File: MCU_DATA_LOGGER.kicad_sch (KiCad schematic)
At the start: 25 parts, among them U1 DS1337S+, U2 24LC1025, U3 24LC1025, U4 ATMEGA328P-AU, Y1 32.768 KHz, Y2 16 MHz

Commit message: fixed all issues
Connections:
- net Vcc: now also BT1.1 (+), C5.1, D3.2 (A), U4.18 (AVCC), U4.4 (VCC)
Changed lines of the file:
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@@
     (effects (font (size 1.27 1.27) bold) (justify right bottom))
+  )
+  (label "Vcc" (at 241.3 43.18 0)
+    (effects (font (size 1.27 1.27) bold) (justify left bottom))
   )
   (label "MOSI" (at 223.52 144.78 180)

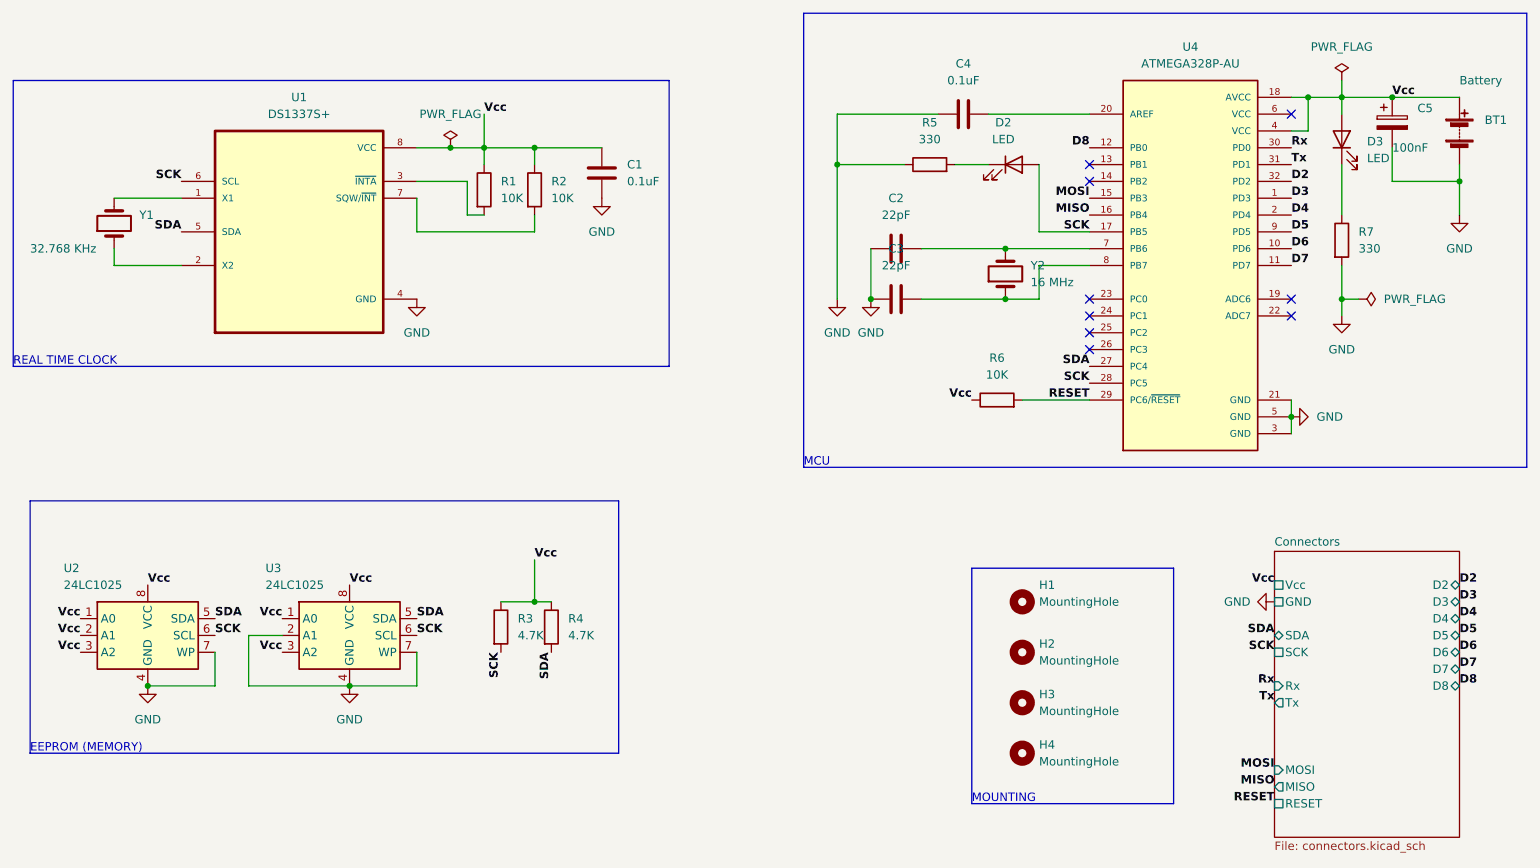
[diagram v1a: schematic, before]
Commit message: sch modification - correction SCL
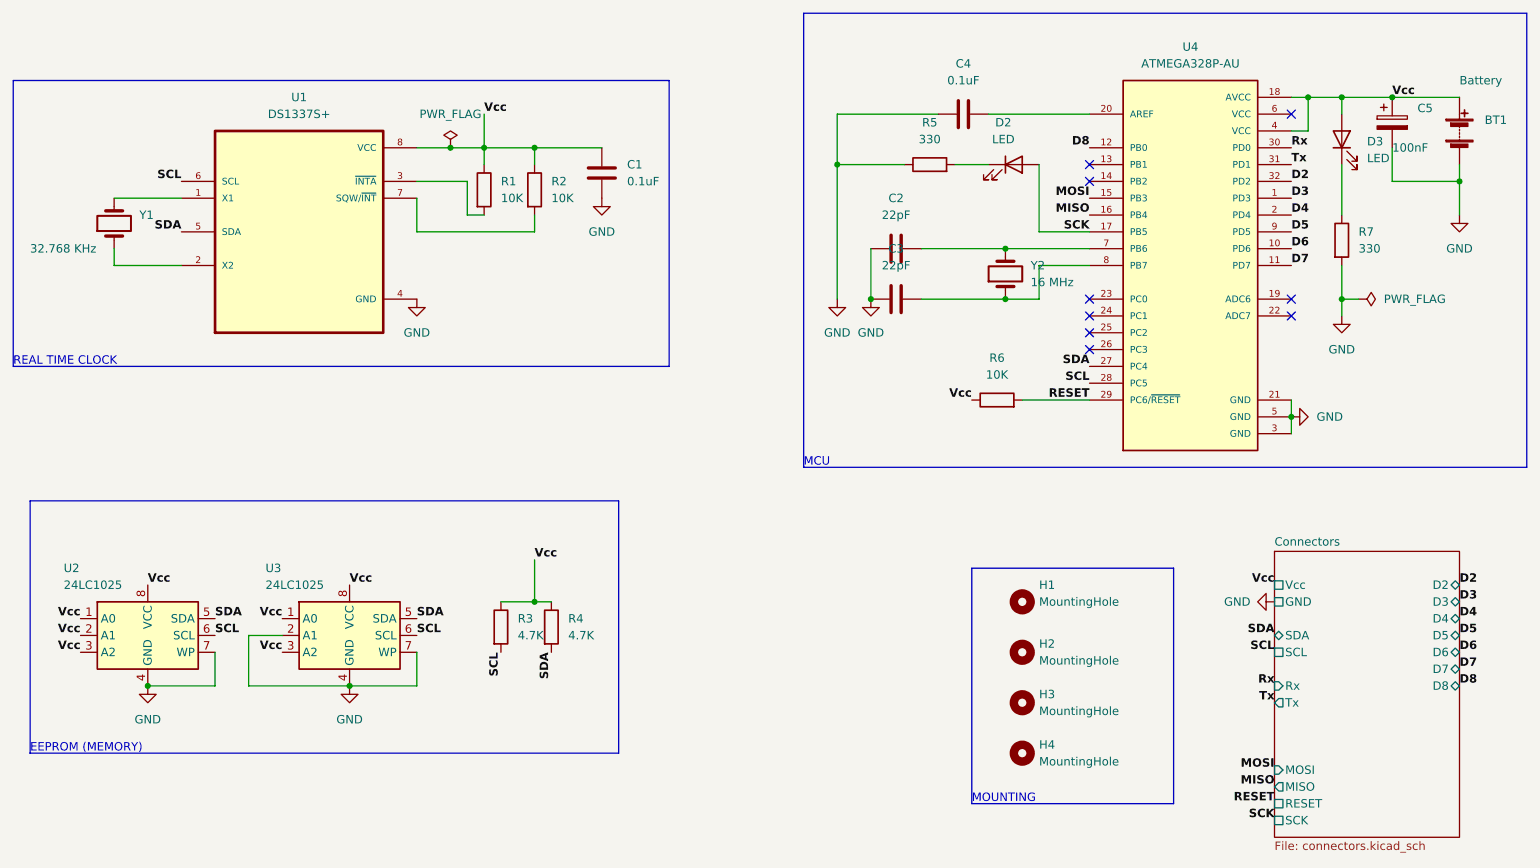
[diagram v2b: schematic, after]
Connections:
- net SCK: no longer R3.2, U1.6 (SCL), U2.6 (SCL), U3.6 (SCL), U4.28 (PC5)
- new net SCL: R3.2, U1.6 (SCL), U2.6 (SCL), U3.6 (SCL), U4.28 (PC5)
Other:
- sheet Connectors ports: added SCL; removed none
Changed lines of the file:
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@@
-    (stroke (width 0) (type default) (color 0 0 0 0))
-  )
-  (wire (pts (xy 233.68 40.64) (xy 233.68 43.18))
     (stroke (width 0) (type default) (color 0 0 0 0))
   )
@@
     (effects (font (size 1.27 1.27) bold) (justify right bottom))
   )
-  (label "SCK" (at 223.52 127 180)
+  (label "SCL" (at 223.52 127 180)
     (effects (font (size 1.27 1.27) bold) (justify right bottom))
   )
@@
     (effects (font (size 1.27 1.27) bold) (justify right bottom))
   )
-  (label "SCK" (at 63.5 124.46 0)
+  (label "SCL" (at 63.5 124.46 0)
     (effects (font (size 1.27 1.27) bold) (justify left bottom))
   )
@@
     (effects (font (size 1.27 1.27) bold) (justify left bottom))
   )
-  (label "SCK" (at 58.42 55.88 180)
+  (label "SCL" (at 58.42 55.88 180)
     (effects (font (size 1.27 1.27) (thickness 0.254) bold) (justify right bottom))
   )
@@
     (effects (font (size 1.27 1.27) bold) (justify right bottom))
   )
-  (label "SCK" (at 195.58 86.36 180)
-    (effects (font (size 1.27 1.27) bold) (justify right bottom))
-  )
-  (label "SCK" (at 106.68 127 270)
+  (label "SCL" (at 195.58 86.36 180)
+    (effects (font (size 1.27 1.27) bold) (justify right bottom))
+  )
+  (label "SCL" (at 106.68 127 270)
     (effects (font (size 1.27 1.27) bold) (justify right bottom))
   )
@@
     (effects (font (size 1.27 1.27) bold) (justify right bottom))
   )
-  (label "SCK" (at 93.98 124.46 0)
-    (effects (font (size 1.27 1.27) bold) (justify left bottom))
+  (label "SCL" (at 93.98 124.46 0)
+    (effects (font (size 1.27 1.27) bold) (justify left bottom))
+  )
+  (label "SCK" (at 223.52 152.4 180)
+    (effects (font (size 1.27 1.27) bold) (justify right bottom))
   )
   (label "SDA" (at 58.42 63.5 180)
@@
     )
     (property "Datasheet" "" (id 3) (at 157.48 73.66 0)
-      (effects (font (size 1.27 1.27)) hide)
-    )
-    (pin "1")
-  )
-  (symbol (lib_id "power:PWR_FLAG") (at 233.68 40.64 0) (unit 1)
-    (in_bom yes) (on_board yes) (fields_autoplaced)
-    (property "Reference" "#FLG0101" (id 0) (at 233.68 38.735 0)
-      (effects (font (size 1.27 1.27)) hide)
-    )
-    (property "Value" "PWR_FLAG" (id 1) (at 233.68 35.56 0))
-    (property "Footprint" "" (id 2) (at 233.68 40.64 0)
-      (effects (font (size 1.27 1.27)) hide)
-    )
-    (property "Datasheet" "~" (id 3) (at 233.68 40.64 0)
       (effects (font (size 1.27 1.27)) hide)
     )
@@
       (effects (font (size 1.27 1.27)) (justify left))
     )
-    (pin "SCK" passive (at 223.52 127 180)
-      (effects (font (size 1.27 1.27)) (justify left))
-    )
     (pin "Rx" input (at 223.52 132.08 180)
       (effects (font (size 1.27 1.27)) (justify left))
@@
     )
     (pin "RESET" passive (at 223.52 149.86 180)
+      (effects (font (size 1.27 1.27)) (justify left))
+    )
+    (pin "SCK" passive (at 223.52 152.4 180)
+      (effects (font (size 1.27 1.27)) (justify left))
+    )
+    (pin "SCL" passive (at 223.52 127 180)
       (effects (font (size 1.27 1.27)) (justify left))
     )
@@
   )
   (symbol_instances
-    (path "/3c9549ae-220b-4d1f-b27a-70cd7a09d053"
-      (reference "#FLG0101") (unit 1) (value "PWR_FLAG") (footprint "")
-    )
     (path "/106dda4b-8523-4300-98fd-27e6bd5b6351"
       (reference "#FLG0102") (unit 1) (value "PWR_FLAG") (footprint "")
